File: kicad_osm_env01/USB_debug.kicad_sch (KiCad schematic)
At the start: 36 parts, among them J5 USB_C_Receptacle_USB2.0, U13 CP2102N-A02-GQFN24, U15 M74VHC1GT14DFT2G, U21 74AUP1T87GWH, U5 SP3003-02JTG

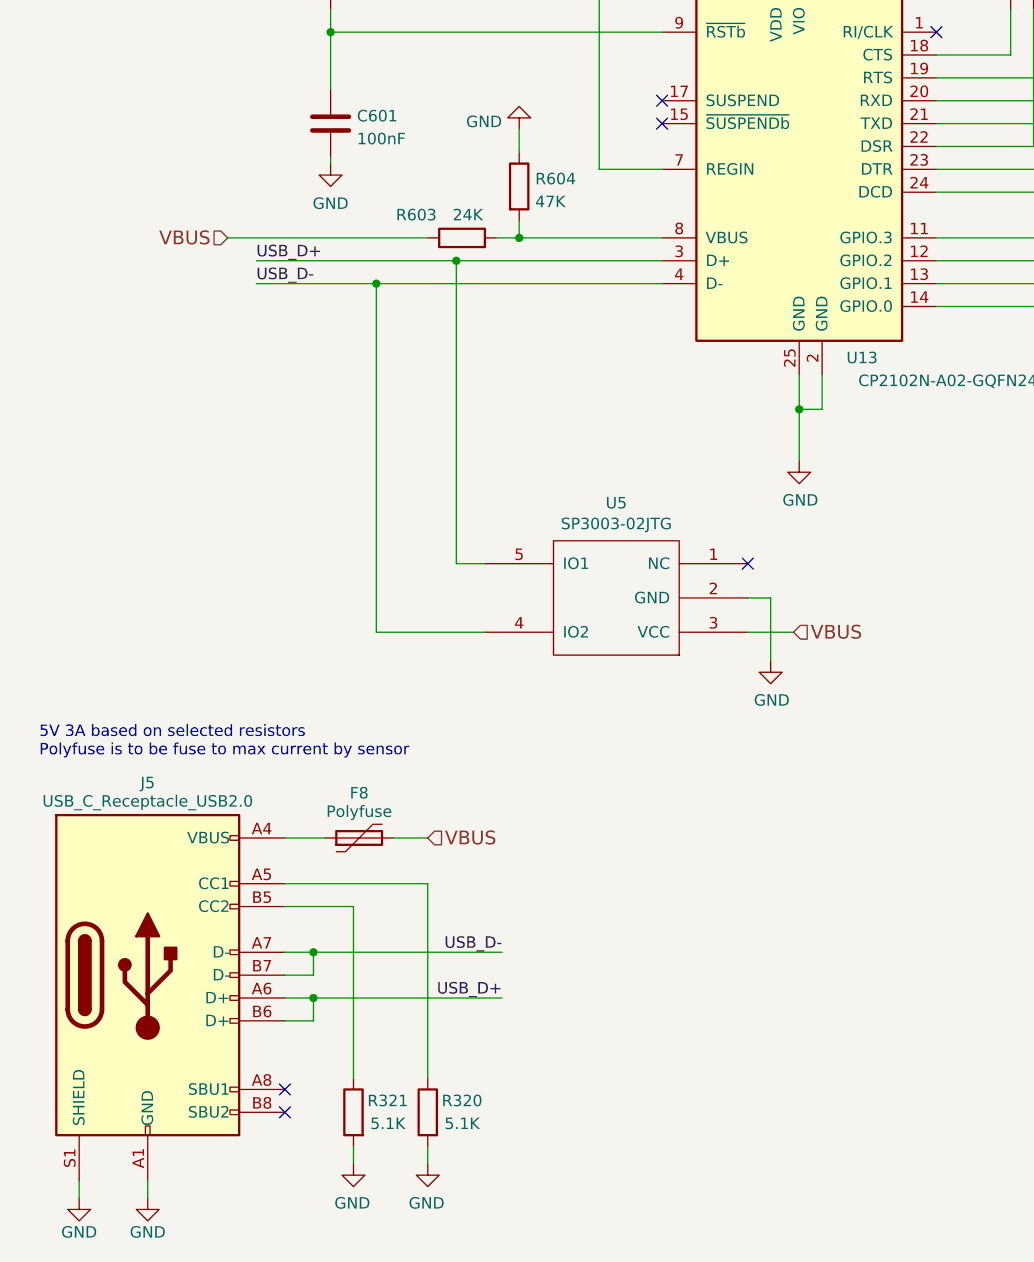
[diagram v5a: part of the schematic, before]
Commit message: updated schematics with 5V ored circuit and new 3v3 regulator
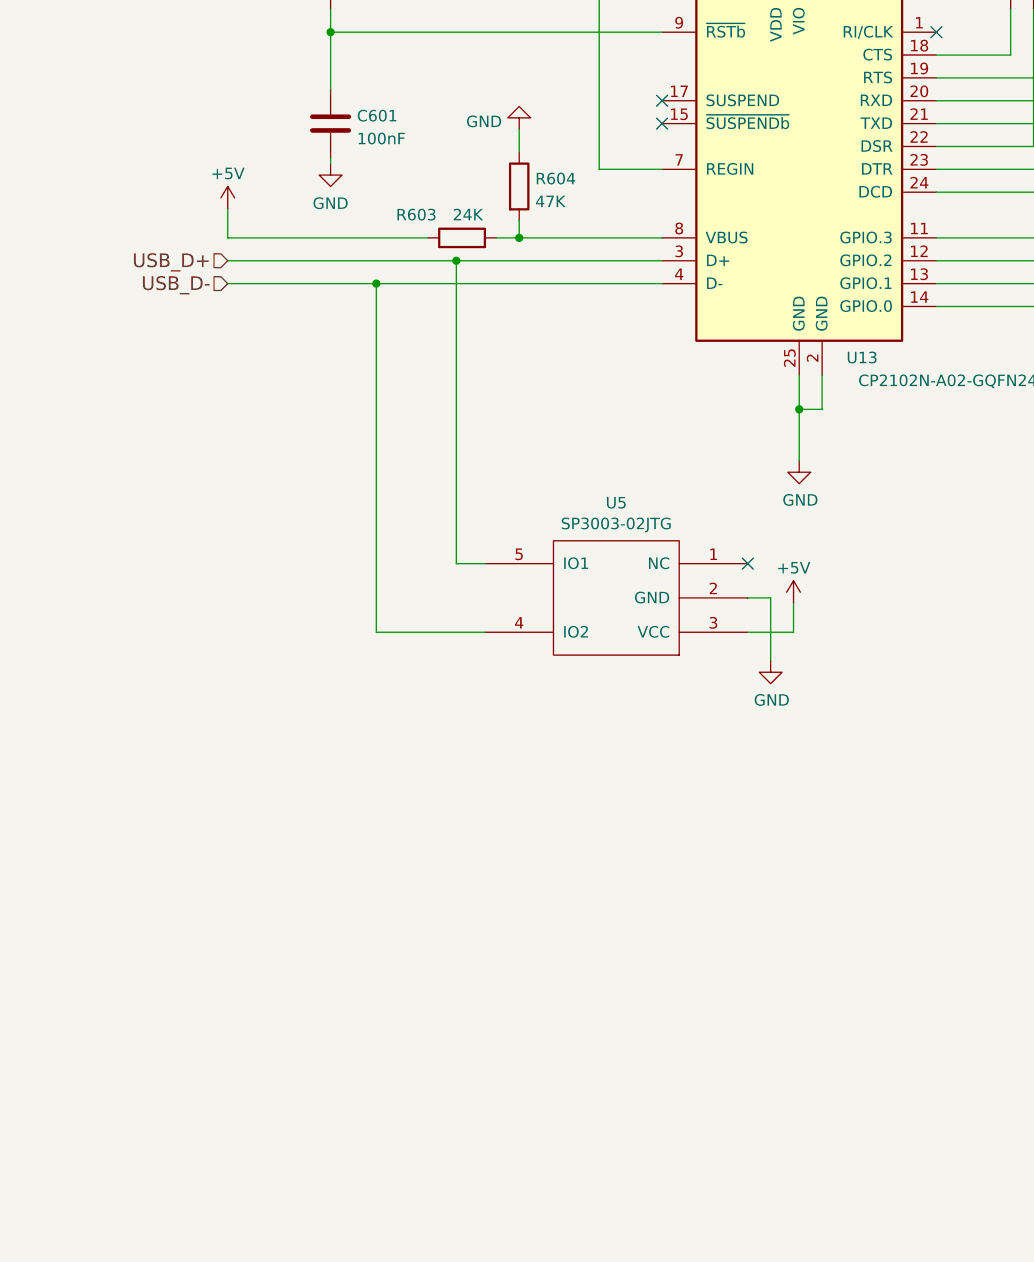
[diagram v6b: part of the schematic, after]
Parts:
- removed F8: Polyfuse, symbol Device:Polyfuse
- removed J5: USB_C_Receptacle_USB2.0, Footprints:MOLEX_216989-0001, symbol Symbols:USB_C_Receptacle_USB2.0
- removed R320, R321: 5.1K, Resistor_SMD:R_0402_1005Metric, symbol Device:R
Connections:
- net VBUS renamed +5V
- no-connect marks 6 -> 4
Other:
- note removed: "5V 3A based on selected resistors Polyfuse is to be fuse to max current by sensor"

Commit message: assigned all footprints
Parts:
- C17, C54, C72: Voltage (none) -> 50V
- C601: Characteristics X5R -> (none); Other Can use own part, but needs to meet the specs -> (none)
- R44, R49, R50, R51, R55, R62, R76, R77, R80, R82: footprint Resistor_SMD:R_0603_1608Metric -> Resistor_SMD:R_0402_1005Metric
- R602, R603, R604: footprint Resistor_SMD:R_0603_1608Metric -> Resistor_SMD:R_0402_1005Metric; Other Can use own part, but needs to meet the specs -> (none); Tolerance 1% -> (none)
- U21: footprint (none) -> Devtank_PCB_lib:tssop-5
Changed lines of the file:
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@@
   (title_block
     (title "Open Smart Monitor")
-    (date "2022-09-26")
-    (rev "C")
+    (date "2023-09-29")
+    (rev "C.2")
     (company "Devtank LTD")
     (comment 1 "Part No: 304-010")
@@
       (effects (font (size 1.27 1.27)) hide)
     )
+    (property "Voltage" "50V" (at 118.11 43.18 0)
+      (effects (font (size 1.27 1.27)) hide)
+    )
     (pin "1")
     (pin "2")
@@
       (effects (font (size 1.27 1.27)))
     )
-    (property "Footprint" "Resistor_SMD:R_0603_1608Metric" (at 144.78 69.088 90)
+    (property "Footprint" "Resistor_SMD:R_0402_1005Metric" (at 144.78 69.088 90)
       (effects (font (size 1.27 1.27)) hide)
     )
@@
       (effects (font (size 1.27 1.27)))
     )
-    (property "Footprint" "Resistor_SMD:R_0603_1608Metric" (at 144.78 71.628 90)
+    (property "Footprint" "Resistor_SMD:R_0402_1005Metric" (at 144.78 71.628 90)
       (effects (font (size 1.27 1.27)) hide)
     )
@@
       (effects (font (size 1.27 1.27)))
     )
-    (property "Footprint" "Resistor_SMD:R_0603_1608Metric" (at 144.78 84.328 90)
+    (property "Footprint" "Resistor_SMD:R_0402_1005Metric" (at 144.78 84.328 90)
       (effects (font (size 1.27 1.27)) hide)
     )
@@
       (effects (font (size 1.27 1.27)))
     )
-    (property "Footprint" "Resistor_SMD:R_0603_1608Metric" (at 144.78 86.868 90)
+    (property "Footprint" "Resistor_SMD:R_0402_1005Metric" (at 144.78 86.868 90)
       (effects (font (size 1.27 1.27)) hide)
     )
@@
       (effects (font (size 1.27 1.27)) hide)
     )
+    (property "Voltage" "50V" (at 235.585 51.435 0)
+      (effects (font (size 1.27 1.27)) hide)
+    )
     (pin "1")
     (pin "2")
@@
       (effects (font (size 1.27 1.27)) (justify left))
     )
-    (property "Footprint" "Resistor_SMD:R_0603_1608Metric" (at 266.065 121.158 90)
+    (property "Footprint" "Resistor_SMD:R_0402_1005Metric" (at 266.065 121.158 90)
       (effects (font (size 1.27 1.27)) hide)
     )
@@
       (effects (font (size 1.27 1.27)) (justify left))
     )
-    (property "Footprint" "Resistor_SMD:R_0603_1608Metric" (at 226.06 158.623 90)
+    (property "Footprint" "Resistor_SMD:R_0402_1005Metric" (at 226.06 158.623 90)
       (effects (font (size 1.27 1.27)) hide)
     )
@@
       (effects (font (size 1.27 1.27)))
     )
-    (property "Footprint" "Resistor_SMD:R_0603_1608Metric" (at 144.78 76.708 90)
+    (property "Footprint" "Resistor_SMD:R_0402_1005Metric" (at 144.78 76.708 90)
       (effects (font (size 1.27 1.27)) hide)
     )
@@
       (effects (font (size 1.27 1.27)) (justify left))
     )
-    (property "Footprint" "Resistor_SMD:R_0603_1608Metric" (at 67.437 76.835 90)
+    (property "Footprint" "Resistor_SMD:R_0402_1005Metric" (at 67.437 76.835 90)
       (effects (font (size 1.27 1.27)) hide)
     )
@@
       (effects (font (size 1.27 1.27)) hide)
     )
-    (property "Tolerance" "1%" (at 69.215 76.835 0)
+    (property "Tolerance" "" (at 69.215 76.835 0)
       (effects (font (size 1.27 1.27)) hide)
     )
@@
       (effects (font (size 1.27 1.27)) hide)
     )
-    (property "Other" "Can use own part, but needs to meet the specs" (at 69.215 76.835 0)
+    (property "Other" "" (at 69.215 76.835 0)
       (effects (font (size 1.27 1.27)) hide)
     )
@@
       (effects (font (size 1.27 1.27)) (justify left))
     )
-    (property "Footprint" "Resistor_SMD:R_0603_1608Metric" (at 264.795 59.563 90)
+    (property "Footprint" "Resistor_SMD:R_0402_1005Metric" (at 264.795 59.563 90)
       (effects (font (size 1.27 1.27)) hide)
     )
@@
       (effects (font (size 1.27 1.27)) hide)
     )
+    (property "Voltage" "50V" (at 230.505 93.98 0)
+      (effects (font (size 1.27 1.27)) hide)
+    )
     (pin "1")
     (pin "2")
@@
       (effects (font (size 1.27 1.27)))
     )
-    (property "Footprint" "Resistor_SMD:R_0603_1608Metric" (at 62.865 84.328 90)
+    (property "Footprint" "Resistor_SMD:R_0402_1005Metric" (at 62.865 84.328 90)
       (effects (font (size 1.27 1.27)) hide)
     )
@@
       (effects (font (size 1.27 1.27)) hide)
     )
-    (property "Tolerance" "1%" (at 62.865 82.55 0)
+    (property "Tolerance" "" (at 62.865 82.55 0)
       (effects (font (size 1.27 1.27)) hide)
     )
@@
       (effects (font (size 1.27 1.27)) hide)
     )
-    (property "Other" "Can use own part, but needs to meet the specs" (at 62.865 82.55 0)
+    (property "Other" "" (at 62.865 82.55 0)
       (effects (font (size 1.27 1.27)) hide)
     )
@@
       (effects (font (size 1.27 1.27)) (justify left))
     )
-    (property "Footprint" "Resistor_SMD:R_0603_1608Metric" (at 46.482 53.34 90)
+    (property "Footprint" "Resistor_SMD:R_0402_1005Metric" (at 46.482 53.34 90)
       (effects (font (size 1.27 1.27)) hide)
     )
@@
       (effects (font (size 1.27 1.27)) hide)
     )
-    (property "Tolerance" "1%" (at 48.26 53.34 0)
+    (property "Tolerance" "" (at 48.26 53.34 0)
       (effects (font (size 1.27 1.27)) hide)
     )
@@
       (effects (font (size 1.27 1.27)) hide)
     )
-    (property "Other" "Can use own part, but needs to meet the specs" (at 48.26 53.34 0)
+    (property "Other" "" (at 48.26 53.34 0)
       (effects (font (size 1.27 1.27)) hide)
     )
@@
       (effects (font (size 1.27 1.27)) (justify left))
     )
-    (property "Footprint" "Resistor_SMD:R_0603_1608Metric" (at 231.775 74.803 90)
+    (property "Footprint" "Resistor_SMD:R_0402_1005Metric" (at 231.775 74.803 90)
       (effects (font (size 1.27 1.27)) hide)
     )
@@
       (effects (font (size 1.27 1.27)) hide)
     )
-    (property "Characteristics" "X5R" (at 48.26 69.85 0)
-      (effects (font (size 1.27 1.27)) hide)
-    )
-    (property "Other" "Can use own part, but needs to meet the specs" (at 48.26 69.85 0)
+    (property "Characteristics" "" (at 48.26 69.85 0)
+      (effects (font (size 1.27 1.27)) hide)
+    )
+    (property "Other" "" (at 48.26 69.85 0)
       (effects (font (size 1.27 1.27)) hide)
     )
@@
       (effects (font (size 1.524 1.524)))
     )
-    (property "Footprint" "" (at 206.375 110.49 0)
+    (property "Footprint" "Devtank_PCB_lib:tssop-5" (at 206.375 110.49 0)
       (effects (font (size 1.27 1.27) italic) hide)
     )
@@
       (effects (font (size 1.27 1.27)))
     )
-    (property "Footprint" "Resistor_SMD:R_0603_1608Metric" (at 144.78 66.548 90)
-      (effects (font (size 1.27 1.27)) hide)
-    )
+    (property "Footprint" "Resistor_SMD:R_0402_1005Metric" (at 144.78 66.548 90)
+      (effects (font (size 1.27 1.27)) hide)
+    )

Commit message: added tracking to layout
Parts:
- removed R44, R55: DNF, Resistor_SMD:R_0402_1005Metric, symbol Device:R
- TP1, TP62, TP63, TP71, TP73, TP74, TP78: footprint TestPoint:TestPoint_THTPad_D1.0mm_Drill0.5mm -> TestPoint:TestPoint_Pad_D1.5mm
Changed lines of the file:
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@@
   (junction (at 252.095 57.785) (diameter 0) (color 0 0 0 0)
   )
-  (junction (at 245.745 57.785) (diameter 0) (color 0 0 0 0)
-  )
   (junction (at 53.34 87.63) (diameter 0) (color 0 0 0 0)
   )
   (junction (at 100.33 48.895) (diameter 0) (color 0 0 0 0)
   )
-  (junction (at 248.285 119.38) (diameter 0) (color 0 0 0 0)
-  )
   (junction (at 253.365 119.38) (diameter 0) (color 0 0 0 0)
   )
@@
   (junction (at 226.695 93.98) (diameter 0) (color 0 0 0 0)
   )
-  (junction (at 205.74 125.095) (diameter 0) (color 0 0 0 0)
-  )
   (junction (at 231.775 51.435) (diameter 0) (color 0 0 0 0)
-  )
-  (junction (at 218.44 57.785) (diameter 0) (color 0 0 0 0)
   )
   (junction (at 100.33 35.56) (diameter 0) (color 0 0 0 0)
@@
     (stroke (width 0) (type default))
   )
-  (wire (pts (xy 205.74 156.845) (xy 222.25 156.845))
-    (stroke (width 0) (type default))
-  )
   (wire (pts (xy 115.57 87.63) (xy 140.97 87.63))
     (stroke (width 0) (type default))
@@
     (stroke (width 0) (type default))
   )
-  (wire (pts (xy 206.375 125.095) (xy 205.74 125.095))
+  (wire (pts (xy 189.23 125.095) (xy 206.375 125.095))
     (stroke (width 0) (type default))
   )
@@
     (stroke (width 0) (type default))
   )
-  (wire (pts (xy 245.745 73.025) (xy 245.745 57.785))
-    (stroke (width 0) (type default))
-  )
-  (wire (pts (xy 218.44 57.785) (xy 221.615 57.785))
-    (stroke (width 0) (type default))
-  )
   (wire (pts (xy 69.215 80.645) (xy 69.215 82.55))
     (stroke (width 0) (type default))
   )
-  (wire (pts (xy 229.87 156.845) (xy 248.285 156.845))
-    (stroke (width 0) (type default))
-  )
   (wire (pts (xy 118.11 35.56) (xy 107.315 35.56))
     (stroke (width 0) (type default))
@@
     (stroke (width 0) (type default))
   )
-  (wire (pts (xy 245.745 57.785) (xy 252.095 57.785))
+  (wire (pts (xy 244.475 57.785) (xy 252.095 57.785))
     (stroke (width 0) (type default))
   )
@@
     (stroke (width 0) (type default))
   )
-  (wire (pts (xy 205.74 125.095) (xy 205.74 156.845))
-    (stroke (width 0) (type default))
-  )
   (wire (pts (xy 231.775 55.245) (xy 231.775 51.435))
     (stroke (width 0) (type default))
@@
     (stroke (width 0) (type default))
   )
-  (wire (pts (xy 247.015 119.38) (xy 248.285 119.38))
+  (wire (pts (xy 247.015 119.38) (xy 253.365 119.38))
     (stroke (width 0) (type default))
   )
@@
     (stroke (width 0) (type default))
   )
-  (wire (pts (xy 218.44 73.025) (xy 218.44 57.785))
-    (stroke (width 0) (type default))
-  )
   (wire (pts (xy 268.605 57.785) (xy 274.955 57.785))
     (stroke (width 0) (type default))
@@
     (stroke (width 0) (type default))
   )
-  (wire (pts (xy 235.585 73.025) (xy 245.745 73.025))
-    (stroke (width 0) (type default))
-  )
   (wire (pts (xy 148.59 85.09) (xy 158.75 85.09))
     (stroke (width 0) (type default))
@@
     (stroke (width 0) (type default))
   )
-  (wire (pts (xy 205.74 125.095) (xy 189.23 125.095))
-    (stroke (width 0) (type default))
-  )
   (wire (pts (xy 36.83 87.63) (xy 53.34 87.63))
     (stroke (width 0) (type default))
@@
     (stroke (width 0) (type default))
   )
-  (wire (pts (xy 218.44 57.785) (xy 201.295 57.785))
-    (stroke (width 0) (type default))
-  )
-  (wire (pts (xy 227.965 73.025) (xy 218.44 73.025))
+  (wire (pts (xy 201.295 57.785) (xy 221.615 57.785))
     (stroke (width 0) (type default))
   )
@@
     (stroke (width 0) (type default))
   )
-  (wire (pts (xy 244.475 57.785) (xy 245.745 57.785))
-    (stroke (width 0) (type default))
-  )
   (polyline (pts (xy 256.413 146.558) (xy 279.908 146.558))
     (stroke (width 0) (type default))
@@
     (stroke (width 0) (type default))
   )
-  (wire (pts (xy 248.285 119.38) (xy 253.365 119.38))
-    (stroke (width 0) (type default))
-  )
   (wire (pts (xy 100.33 35.56) (xy 100.33 45.72))
     (stroke (width 0) (type default))
@@
   )
   (wire (pts (xy 118.11 39.37) (xy 118.11 35.56))
-    (stroke (width 0) (type default))
-  )
-  (wire (pts (xy 248.285 156.845) (xy 248.285 119.38))
     (stroke (width 0) (type default))
   )
@@
       (effects (font (size 1.27 1.27)) (justify left) hide)
     )
-    (property "Footprint" "TestPoint:TestPoint_THTPad_D1.0mm_Drill0.5mm" (at 128.905 57.15 0)
+    (property "Footprint" "TestPoint:TestPoint_Pad_D1.5mm" (at 128.905 57.15 0)
       (effects (font (size 1.27 1.27)) hide)
     )
@@
         (path "/ab8b0540-9c9f-4195-88f5-7bed0b0a8ed6/00000000-0000-0000-0000-00005f4610be"
           (reference "#PWR050") (unit 1)
-        )
-      )
-    )
-  )
-  (symbol (lib_id "Device:R") (at 226.06 156.845 90) (unit 1)
-    (in_bom yes) (on_board yes) (dnp no)
-    (property "Reference" "R44" (at 220.98 155.575 90)
-      (effects (font (size 1.27 1.27)) (justify left))
-    )
-    (property "Value" "DNF" (at 233.045 156.21 90)
-      (effects (font (size 1.27 1.27)) (justify left))
-    )
-    (property "Footprint" "Resistor_SMD:R_0402_1005Metric" (at 226.06 158.623 90)
-      (effects (font (size 1.27 1.27)) hide)
-    )
-    (property "Datasheet" "" (at 226.06 156.845 0)
-      (effects (font (size 1.27 1.27)) hide)
-    )
-    (pin "1")
-    (pin "2")
-    (instances
-      (project "OSM_env01"
-        (path "/ab8b0540-9c9f-4195-88f5-7bed0b0a8ed6/00000000-0000-0000-0000-00005f4610be"
-          (reference "R44") (unit 1)
         )
       )
@@
       (effects (font (size 1.27 1.27)) (justify left) hide)
     )
-    (property "Footprint" "TestPoint:TestPoint_THTPad_D1.0mm_Drill0.5mm" (at 258.445 115.57 0)
+    (property "Footprint" "TestPoint:TestPoint_Pad_D1.5mm" (at 258.445 115.57 0)
       (effects (font (size 1.27 1.27)) hide)
     )
@@
       (effects (font (size 1.27 1.27)) (justify left) hide)
     )
-    (property "Footprint" "TestPoint:TestPoint_THTPad_D1.0mm_Drill0.5mm" (at 165.735 69.85 0)
+    (property "Footprint" "TestPoint:TestPoint_Pad_D1.5mm" (at 165.735 69.85 0)
       (effects (font (size 1.27 1.27)) hide)
     )
@@
       (effects (font (size 1.27 1.27)) (justify left) hide)
     )
-    (property "Footprint" "TestPoint:TestPoint_THTPad_D1.0mm_Drill0.5mm" (at 131.445 57.15 0)
+    (property "Footprint" "TestPoint:TestPoint_Pad_D1.5mm" (at 131.445 57.15 0)
       (effects (font (size 1.27 1.27)) hide)
     )
@@
       (effects (font (size 1.27 1.27)) (justify left) hide)
     )
-    (property "Footprint" "TestPoint:TestPoint_THTPad_D1.0mm_Drill0.5mm" (at 257.175 53.975 0)
+    (property "Footprint" "TestPoint:TestPoint_Pad_D1.5mm" (at 257.175 53.975 0)
       (effects (font (size 1.27 1.27)) hide)
     )
@@
       (effects (font (size 1.27 1.27)) (justify left) hide)
     )
-    (property "Footprint" "TestPoint:TestPoint_THTPad_D1.0mm_Drill0.5mm" (at 165.735 80.01 0)
+    (property "Footprint" "TestPoint:TestPoint_Pad_D1.5mm" (at 165.735 80.01 0)
       (effects (font (size 1.27 1.27)) hide)
     )
@@
         (path "/ab8b0540-9c9f-4195-88f5-7bed0b0a8ed6/00000000-0000-0000-0000-00005f4610be"
           (reference "TP63") (unit 1)
-        )
-      )
-    )
-  )
-  (symbol (lib_id "Device:R") (at 231.775 73.025 90) (unit 1)
-    (in_bom yes) (on_board yes) (dnp no)
-    (property "Reference" "R55" (at 226.695 71.755 90)
-      (effects (font (size 1.27 1.27)) (justify left))
-    )
-    (property "Value" "DNF" (at 238.76 72.39 90)
-      (effects (font (size 1.27 1.27)) (justify left))
-    )
-    (property "Footprint" "Resistor_SMD:R_0402_1005Metric" (at 231.775 74.803 90)
-      (effects (font (size 1.27 1.27)) hide)
-    )
-    (property "Datasheet" "" (at 231.775 73.025 0)
-      (effects (font (size 1.27 1.27)) hide)
-    )
-    (pin "1")
-    (pin "2")
-    (instances
-      (project "OSM_env01"
-        (path "/ab8b0540-9c9f-4195-88f5-7bed0b0a8ed6/00000000-0000-0000-0000-00005f4610be"
-          (reference "R55") (unit 1)
         )
       )
@@
       (effects (font (size 1.27 1.27)) (justify left) hide)
     )
-    (property "Footprint" "TestPoint:TestPoint_THTPad_D1.0mm_Drill0.5mm" (at 133.985 57.15 0)
-      (effects (font (size 1.27 1.27)) hide)
-    )
+    (property "Footprint" "TestPoint:TestPoint_Pad_D1.5mm" (at 133.985 57.15 0)
+      (effects (font (size 1.27 1.27)) hide)
+    )
